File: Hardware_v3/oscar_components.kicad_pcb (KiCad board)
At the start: 4 copper layers, 71 x 100 mm, 71 parts, among them J1 SWD_Header, J10 MIDI_THROUGH, J11 USB_C_Receptacle, J12 Debug, J2 Eurorack_10_pin_power, J3 ChannelC_In, J4 ChannelA_In, J5 ChannelB_In, J6 ChC_Buff_Out, J7 ChA_Buff_Out, J8 ChB_Buff_Out, J9 MIDI_IN, SW1 Reset_Button, SW2 Menu_Button, SW3 Left_Encoder, SW4 Right_Encoder, U1 LT1117-3.3, U2 ILI9341_SPI_Daughterboard, U3 STM32F446RETx, U4 TL074, U5 MCP6004, U6 H11L1, Y1 8MHz

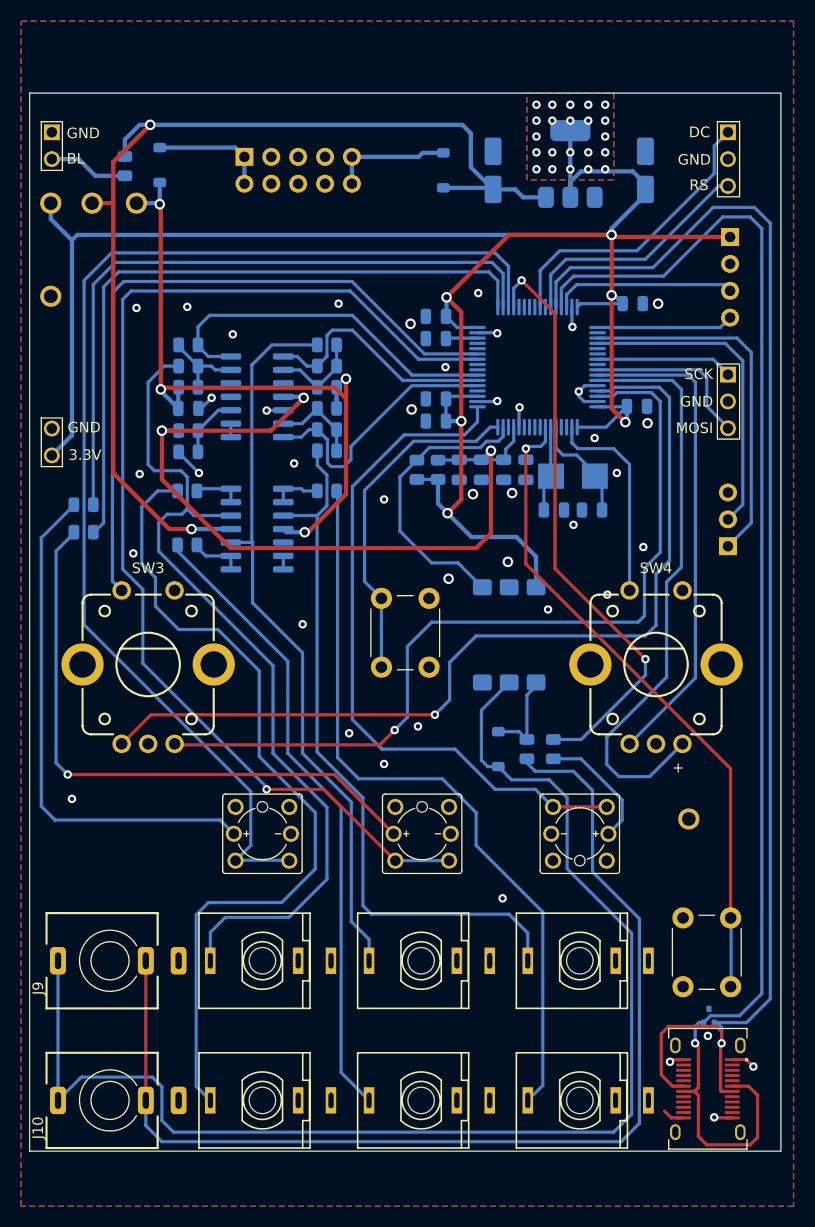
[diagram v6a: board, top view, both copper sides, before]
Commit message: V3 production files submitted to JLC
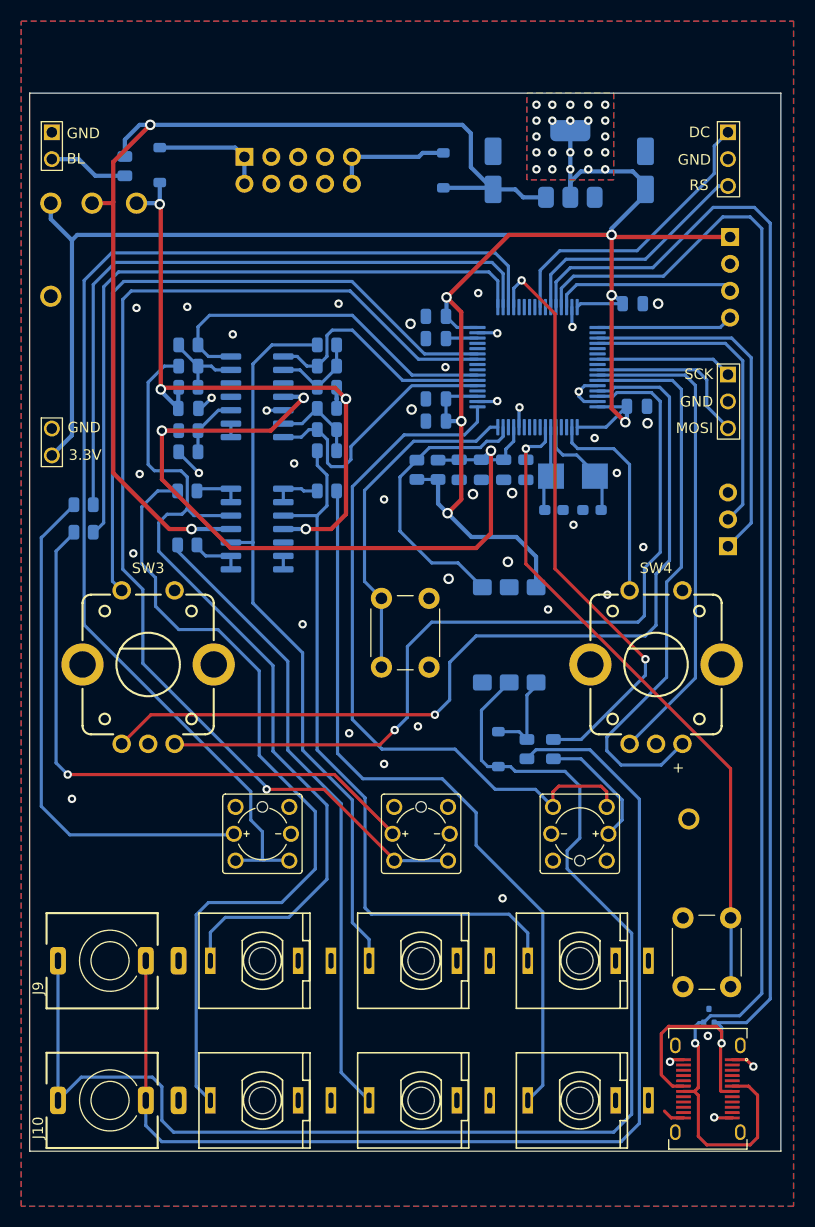
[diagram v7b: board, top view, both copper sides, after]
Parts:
- C4, C5: footprint Capacitor_SMD:C_0805_2012Metric -> Capacitor_SMD:C_0603_1608Metric_Pad1.08x0.95mm_HandSolder
- J12: value Debug -> Debug_Header
- R10, R8, R9: value 14k -> 15k
- moved BTN2 0.10 mm to (137.0, 120.0)
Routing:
- net /ChC_Button: track 65.2 -> 68.5 mm
- net /MIDI_VREF: track 104.5 -> 107.1 mm
- net /MIDI_DATA: track 123.5 -> 125.8 mm
- net /R_ENC_DN: track 55.6 -> 53.9 mm

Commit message: Updated LED resistor values
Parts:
- R18, R19, R20: value 560 -> 1.5k
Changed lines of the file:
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@@
 			)
 		)
-		(property "Value" "560"
+		(property "Value" "1.5k"
 			(at 0 -1.65 90)
 			(layer "B.Fab")
@@
 			)
 		)
-		(property "Value" "560"
+		(property "Value" "1.5k"
 			(at 0 -1.65 0)
 			(layer "B.Fab")
@@
 			)
 		)
-		(property "Value" "560"
+		(property "Value" "1.5k"
 			(at 0 -1.65 0)
 			(layer "B.Fab")
